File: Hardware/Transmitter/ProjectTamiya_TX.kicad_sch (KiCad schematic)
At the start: 43 parts, among them J1 Boot, J10 NRF, J11 NRF_power, J2 Power, J3 Serial, J4 Steering, J5 Throttle, J6 ENC1, J7 OLED, J8 ENC2, J9 Debug, Q1 2N7002BK, Q2 2N7002BK, Q3 2N7002BK, SW1 Reset, SW2 Switch, U1 STM32F303CCT6, U2 AP2111H-3.3TRG1, Y1 XT324 [20pF, 12MHz]

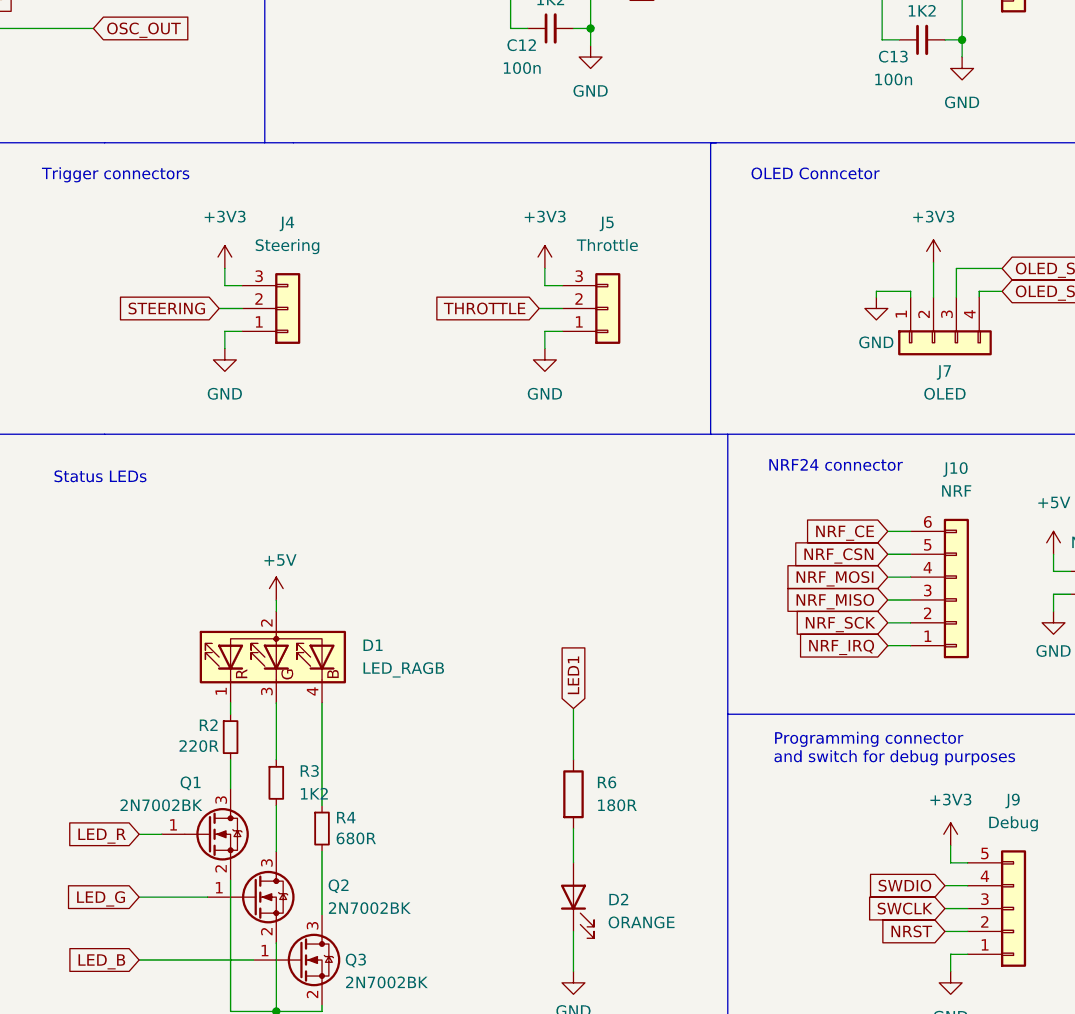
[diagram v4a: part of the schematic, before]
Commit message: Minor schematic corrections
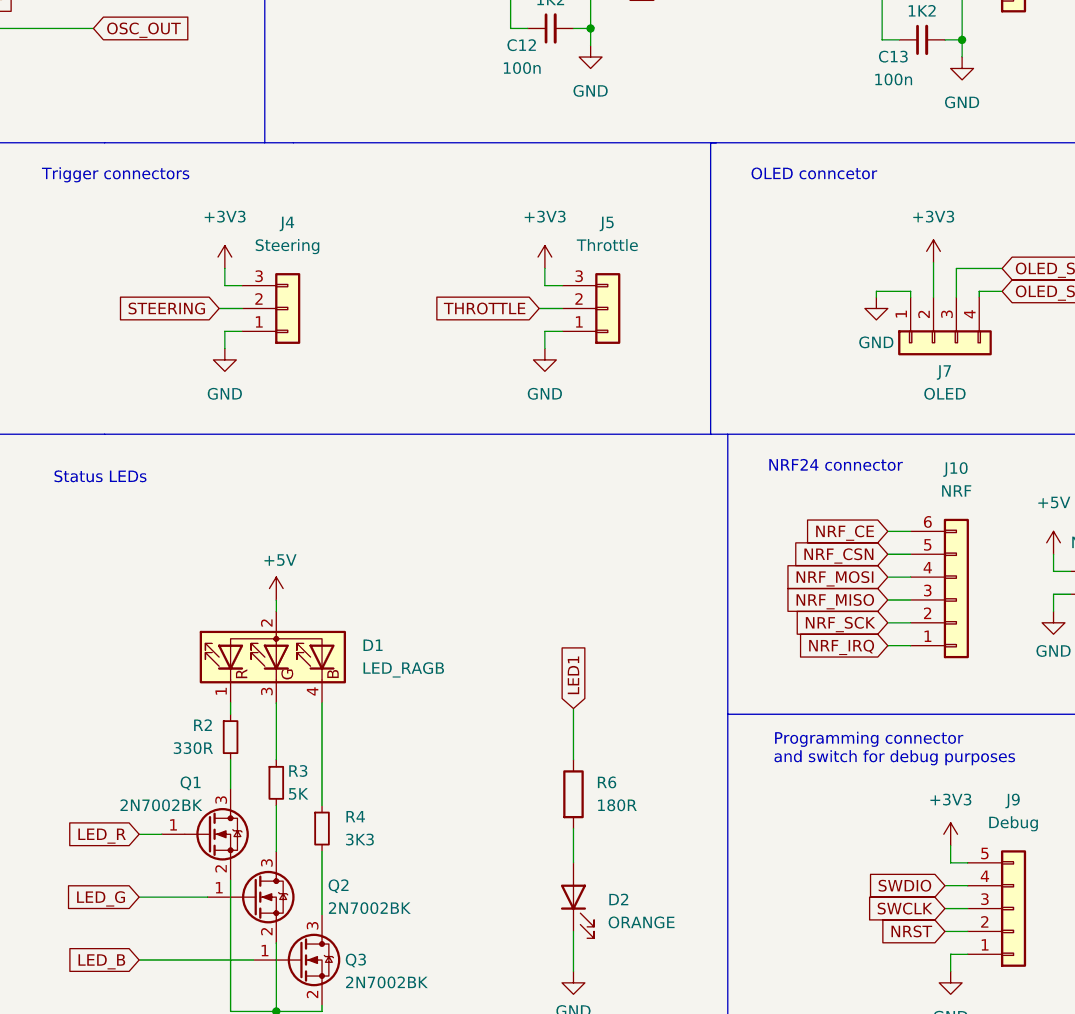
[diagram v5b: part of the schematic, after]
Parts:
- R2: value 220R -> 330R
- R3: value 1K2 -> 5K
- R4: value 680R -> 3K3
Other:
- note added: "OLED conncetor"
- note removed: "OLED Conncetor"
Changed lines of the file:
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@@
     (effects (font (size 1.27 1.27)) (justify left bottom))
   )
-  (text "OLED Conncetor" (at 238.125 52.07 0)
+  (text "OLED conncetor" (at 238.125 52.07 0)
     (effects (font (size 1.27 1.27)) (justify left bottom))
   )
@@
   )
   (symbol (lib_id "Device:R_Small") (at 185.42 118.745 0) (unit 1)
-    (in_bom yes) (on_board yes) (fields_autoplaced)
-    (property "Reference" "R3" (id 0) (at 187.96 117.4749 0)
-      (effects (font (size 1.27 1.27)) (justify left))
-    )
-    (property "Value" "1K2" (id 1) (at 187.96 120.0149 0)
+    (in_bom yes) (on_board yes)
+    (property "Reference" "R3" (id 0) (at 186.69 117.475 0)
+      (effects (font (size 1.27 1.27)) (justify left))
+    )
+    (property "Value" "5K" (id 1) (at 186.69 120.015 0)
       (effects (font (size 1.27 1.27)) (justify left))
     )
@@
   (symbol (lib_id "Device:R_Small") (at 190.5 123.825 0) (unit 1)
     (in_bom yes) (on_board yes) (fields_autoplaced)
-    (property "Reference" "R4" (id 0) (at 191.9986 122.6566 0)
-      (effects (font (size 1.27 1.27)) (justify left))
-    )
-    (property "Value" "680R" (id 1) (at 191.9986 124.968 0)
+    (property "Reference" "R4" (id 0) (at 193.04 122.5549 0)
+      (effects (font (size 1.27 1.27)) (justify left))
+    )
+    (property "Value" "3K3" (id 1) (at 193.04 125.0949 0)
       (effects (font (size 1.27 1.27)) (justify left))
     )
@@
   )
   (symbol (lib_id "Device:R_Small") (at 180.34 113.665 0) (unit 1)
-    (in_bom yes) (on_board yes) (fields_autoplaced)
-    (property "Reference" "R2" (id 0) (at 179.07 112.395 0)
+    (in_bom yes) (on_board yes)
+    (property "Reference" "R2" (id 0) (at 178.435 112.395 0)
       (effects (font (size 1.27 1.27)) (justify right))
     )
-    (property "Value" "220R" (id 1) (at 179.07 114.7064 0)
+    (property "Value" "330R" (id 1) (at 178.435 114.935 0)
       (effects (font (size 1.27 1.27)) (justify right))
     )
@@
     )
     (path "/278d76c6-3cbe-4c0a-8a52-5aab1a12a5f9"
-      (reference "R2") (unit 1) (value "220R") (footprint "Resistor_THT:R_Axial_DIN0204_L3.6mm_D1.6mm_P2.54mm_Vertical")
+      (reference "R2") (unit 1) (value "330R") (footprint "Resistor_THT:R_Axial_DIN0204_L3.6mm_D1.6mm_P2.54mm_Vertical")
     )
     (path "/03026317-2766-4e4a-ab9f-3018667426f9"
-      (reference "R3") (unit 1) (value "1K2") (footprint "Resistor_THT:R_Axial_DIN0204_L3.6mm_D1.6mm_P2.54mm_Vertical")
+      (reference "R3") (unit 1) (value "5K") (footprint "Resistor_THT:R_Axial_DIN0204_L3.6mm_D1.6mm_P2.54mm_Vertical")
     )
     (path "/162941cf-b3d6-48bb-a349-a848b87c4e93"
-      (reference "R4") (unit 1) (value "680R") (footprint "Resistor_THT:R_Axial_DIN0204_L3.6mm_D1.6mm_P2.54mm_Vertical")
+      (reference "R4") (unit 1) (value "3K3") (footprint "Resistor_THT:R_Axial_DIN0204_L3.6mm_D1.6mm_P2.54mm_Vertical")
     )
     (path "/fdf29986-0aa3-4268-a25a-bd25c7bec492"

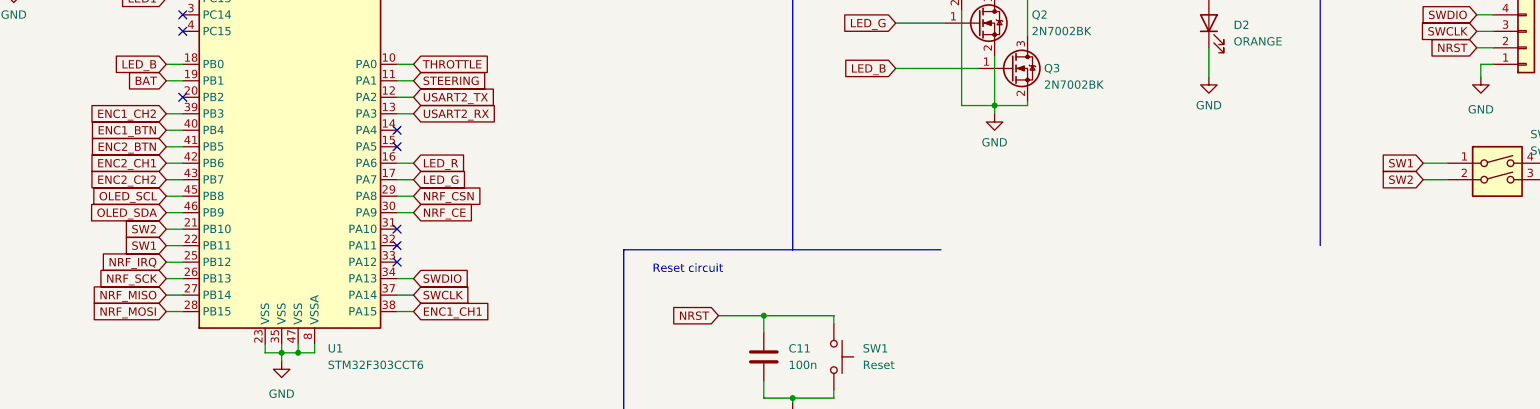
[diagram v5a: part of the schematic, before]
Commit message: Corrected labels to reflect real hardware (DIP switch)
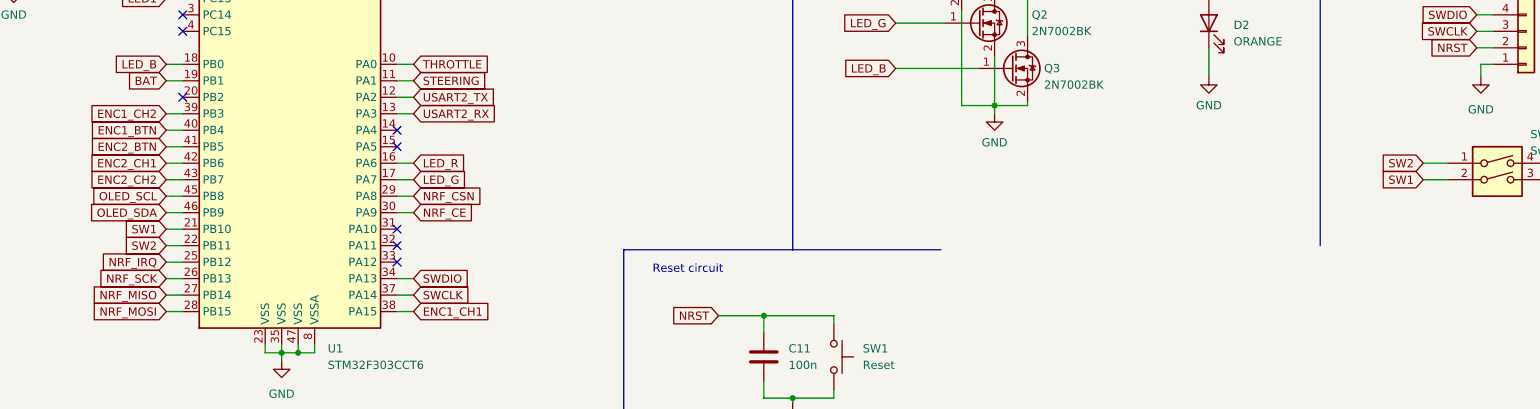
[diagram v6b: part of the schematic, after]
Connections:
- net SW1: now also SW2.2, U1.21 (PB10); no longer SW2.1, U1.22 (PB11)
- net SW2: now also SW2.1, U1.22 (PB11); no longer SW2.2, U1.21 (PB10)
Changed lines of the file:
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@@
     )
   )
-  (global_label "SW1" (shape input) (at 251.46 153.035 180) (fields_autoplaced)
-    (effects (font (size 1.27 1.27)) (justify right))
-    (property "Intersheet References" "${INTERSHEET_REFS}" (id 0) (at 245.1764 152.9556 0)
+  (global_label "SW1" (shape input) (at 251.46 155.575 180) (fields_autoplaced)
+    (effects (font (size 1.27 1.27)) (justify right))
+    (property "Intersheet References" "${INTERSHEET_REFS}" (id 0) (at 245.1764 155.6544 0)
       (effects (font (size 1.27 1.27)) (justify right) hide)
     )
@@
     )
   )
-  (global_label "SW1" (shape input) (at 57.785 165.735 180) (fields_autoplaced)
-    (effects (font (size 1.27 1.27)) (justify right))
-    (property "Intersheet References" "${INTERSHEET_REFS}" (id 0) (at 51.5014 165.6556 0)
+  (global_label "SW1" (shape input) (at 57.785 163.195 180) (fields_autoplaced)
+    (effects (font (size 1.27 1.27)) (justify right))
+    (property "Intersheet References" "${INTERSHEET_REFS}" (id 0) (at 51.5014 163.2744 0)
       (effects (font (size 1.27 1.27)) (justify right) hide)
     )
@@
     )
   )
-  (global_label "SW2" (shape input) (at 251.46 155.575 180) (fields_autoplaced)
-    (effects (font (size 1.27 1.27)) (justify right))
-    (property "Intersheet References" "${INTERSHEET_REFS}" (id 0) (at 245.1764 155.4956 0)
+  (global_label "SW2" (shape input) (at 251.46 153.035 180) (fields_autoplaced)
+    (effects (font (size 1.27 1.27)) (justify right))
+    (property "Intersheet References" "${INTERSHEET_REFS}" (id 0) (at 245.1764 153.1144 0)
       (effects (font (size 1.27 1.27)) (justify right) hide)
     )
@@
     )
   )
-  (global_label "SW2" (shape input) (at 57.785 163.195 180) (fields_autoplaced)
-    (effects (font (size 1.27 1.27)) (justify right))
-    (property "Intersheet References" "${INTERSHEET_REFS}" (id 0) (at 51.5014 163.1156 0)
-      (effects (font (size 1.27 1.27)) (justify right) hide)
-    )
+  (global_label "SW2" (shape input) (at 57.785 165.735 180) (fields_autoplaced)
+    (effects (font (size 1.27 1.27)) (justify right))
+    (property "Intersheet References" "${INTERSHEET_REFS}" (id 0) (at 51.5014 165.8144 0)
+      (effects (font (size 1.27 1.27)) (justify right) hide)
+    )
